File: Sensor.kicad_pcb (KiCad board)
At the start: 2 copper layers, 49.5 x 49.5 mm, 51 parts, among them IC1 STM32L051K8T6, P1 CONN_02X04, P3 CONN_02X04, P4 CONN_01X04, P5 CONN_01X02, Q1 PMosfetGen, Q2 PMosfetGen, Q4 PMosfetGen, Q5 AO3401, SW1 SW_PUSH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

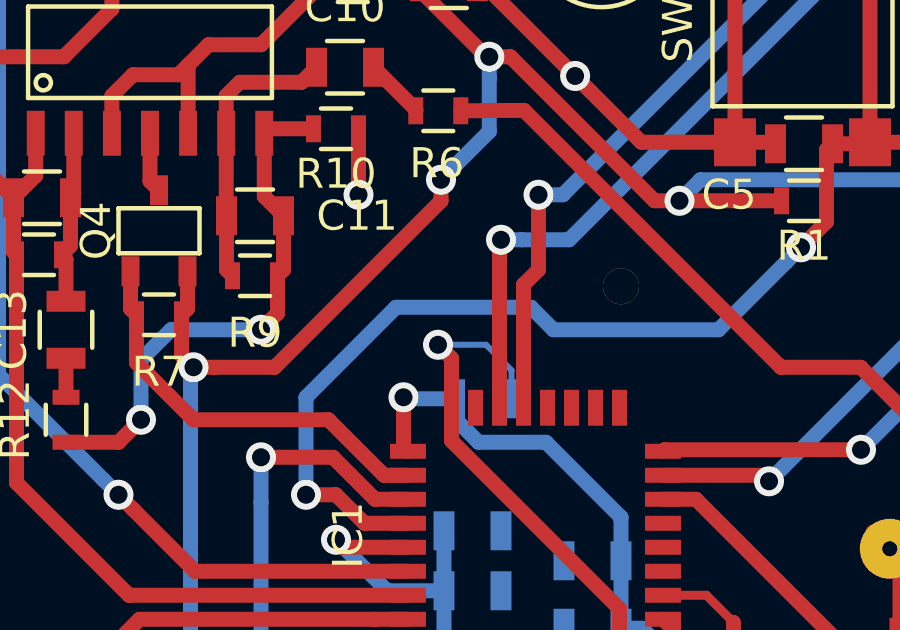
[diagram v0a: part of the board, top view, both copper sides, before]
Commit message: Fix Boot0 pin and add prices per component
Signed-off-by: Philip Luyckx <philip.luyckx@gmail.com>
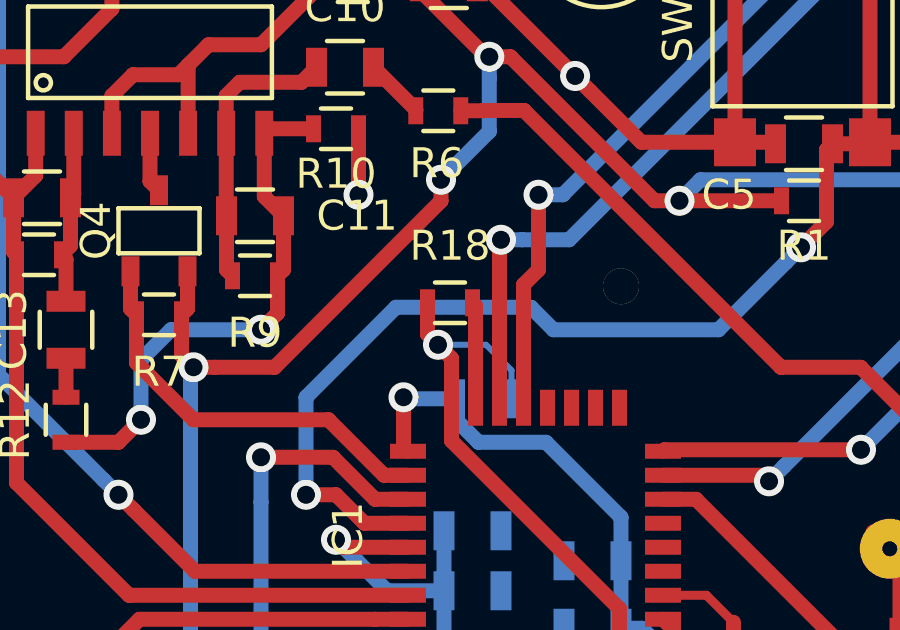
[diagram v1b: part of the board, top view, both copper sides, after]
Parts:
- added R18: 475, Resistors_SMD:R_0603, F.Cu at (137.8, 84.6)
- C12, C15: value C -> 100nF
- Q1, Q2, Q4: value PMosfetGen -> AO3401
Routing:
- net Net-(IC1-Pad31): track 0.00 -> 3.54 mm
- net GND: track 151.5 -> 153.0 mm
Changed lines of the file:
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@@
 (kicad_pcb (version 4) (host pcbnew 4.0.2-4+6225~38~ubuntu15.10.1-stable)
   (general
-    (links 115)
+    (links 117)
     (no_connects 0)
-    (area 109.774999 55.61 191.5 119.575)
+    (area 118.449999 69.199999 168.050001 118.800001)
     (thickness 1.6)
     (drawings 10)
-    (tracks 460)
+    (tracks 464)
     (zones 0)
-    (modules 51)
+    (modules 52)
     (nets 46)
   )
@@
       (effects (font (size 1 1) (thickness 0.15)))
     )
-    (fp_text value C (at 0 2.1) (layer F.Fab)
+    (fp_text value 100nF (at 0 2.1) (layer F.Fab)
       (effects (font (size 1 1) (thickness 0.15)))
     )
@@
       (effects (font (size 1 1) (thickness 0.15)))
     )
-    (fp_text value PMosfetGen (at 0.05 0.05 90) (layer F.Fab) hide
+    (fp_text value AO3401 (at 0.05 0.05 90) (layer F.Fab) hide
       (effects (font (size 1 1) (thickness 0.15)))
     )
@@
       (effects (font (size 1 1) (thickness 0.15)))
     )
-    (fp_text value PMosfetGen (at 0.05 0.05 90) (layer F.Fab) hide
+    (fp_text value AO3401 (at 0.05 0.05 90) (layer F.Fab) hide
       (effects (font (size 1 1) (thickness 0.15)))
     )
@@
       (effects (font (size 1 1) (thickness 0.15)))
     )
-    (fp_text value PMosfetGen (at 0.05 0.05) (layer F.Fab) hide
+    (fp_text value AO3401 (at 0.05 0.05) (layer F.Fab) hide
       (effects (font (size 1 1) (thickness 0.15)))
     )
@@
       (effects (font (size 1 1) (thickness 0.15)))
     )
-    (fp_text value C (at 0 2.1) (layer F.Fab)
+    (fp_text value 100nF (at 0 2.1) (layer F.Fab)
       (effects (font (size 1 1) (thickness 0.15)))
     )
@@
       (net 1 +BATT))
     (model Resistors_SMD.3dshapes/R_0805.wrl
+      (at (xyz 0 0 0))
+      (scale (xyz 1 1 1))
+      (rotate (xyz 0 0 0))
+    )
+  )
+  (module Resistors_SMD:R_0603 (layer F.Cu)
+    (at 137.8 84.6)
+    (descr "Resistor SMD 0603, reflow soldering, Vishay (see dcrcw.pdf)")
+    (tags "resistor 0603")
+    (attr smd)
+    (fp_text reference R18 (at 0 -1.9) (layer F.SilkS)
+      (effects (font (size 1 1) (thickness 0.15)))
+    )
+    (fp_text value 475 (at 0 1.9) (layer F.Fab)
+      (effects (font (size 1 1) (thickness 0.15)))
+    )
+    (fp_line (start -1.3 -0.8) (end 1.3 -0.8) (layer F.CrtYd) (width 0.05))
+    (fp_line (start -1.3 0.8) (end 1.3 0.8) (layer F.CrtYd) (width 0.05))
+    (fp_line (start -1.3 -0.8) (end -1.3 0.8) (layer F.CrtYd) (width 0.05))
+    (fp_line (start 1.3 -0.8) (end 1.3 0.8) (layer F.CrtYd) (width 0.05))
+    (fp_line (start 0.5 0.675) (end -0.5 0.675) (layer F.SilkS) (width 0.15))
+    (fp_line (start -0.5 -0.675) (end 0.5 -0.675) (layer F.SilkS) (width 0.15))
+    (pad 1 smd rect (at -0.75 0) (size 0.5 0.9) (layers F.Cu F.Paste F.Mask)
+      (net 2 GND))
+    (pad 2 smd rect (at 0.75 0) (size 0.5 0.9) (layers F.Cu F.Paste F.Mask)
+      (net 39 "Net-(IC1-Pad31)"))
+    (model Resistors_SMD.3dshapes/R_0603.wrl
       (at (xyz 0 0 0))
       (scale (xyz 1 1 1))
@@
   (segment (start 138.568665 116.340649) (end 134.340649 116.340649) (width 0.5) (layer B.Cu) (net 1))
   (segment (start 134.340649 116.340649) (end 133 115) (width 0.5) (layer B.Cu) (net 1))
+  (segment (start 137.05 84.6) (end 137.05 85.65) (width 0.5) (layer F.Cu) (net 2))
+  (segment (start 137.05 85.65) (end 137.4 86) (width 0.5) (layer F.Cu) (net 2))
   (segment (start 138.71 73.9) (end 138.83 73.9) (width 0.5) (layer F.Cu) (net 2))
   (segment (start 138.83 73.9) (end 141.97 77.04) (width 0.5) (layer F.Cu) (net 2))
@@
   (segment (start 126.53 77.7) (end 127.23 77) (width 0.5) (layer F.Cu) (net 35))
   (segment (start 133.81 73.9) (end 133.81 71.9) (width 0.5) (layer F.Cu) (net 35))
+  (segment (start 138.65 88.1) (end 138.65 84.7) (width 0.5) (layer F.Cu) (net 39))
+  (segment (start 138.65 84.7) (end 138.55 84.6) (width 0.5) (layer F.Cu) (net 39))
   (segment (start 127.15 83.55) (end 127.15 84.8) (width 0.5) (layer F.Cu) (net 41))
   (segment (start 127.15 84.8) (end 127.35 85) (width 0.5) (layer F.Cu) (net 41))

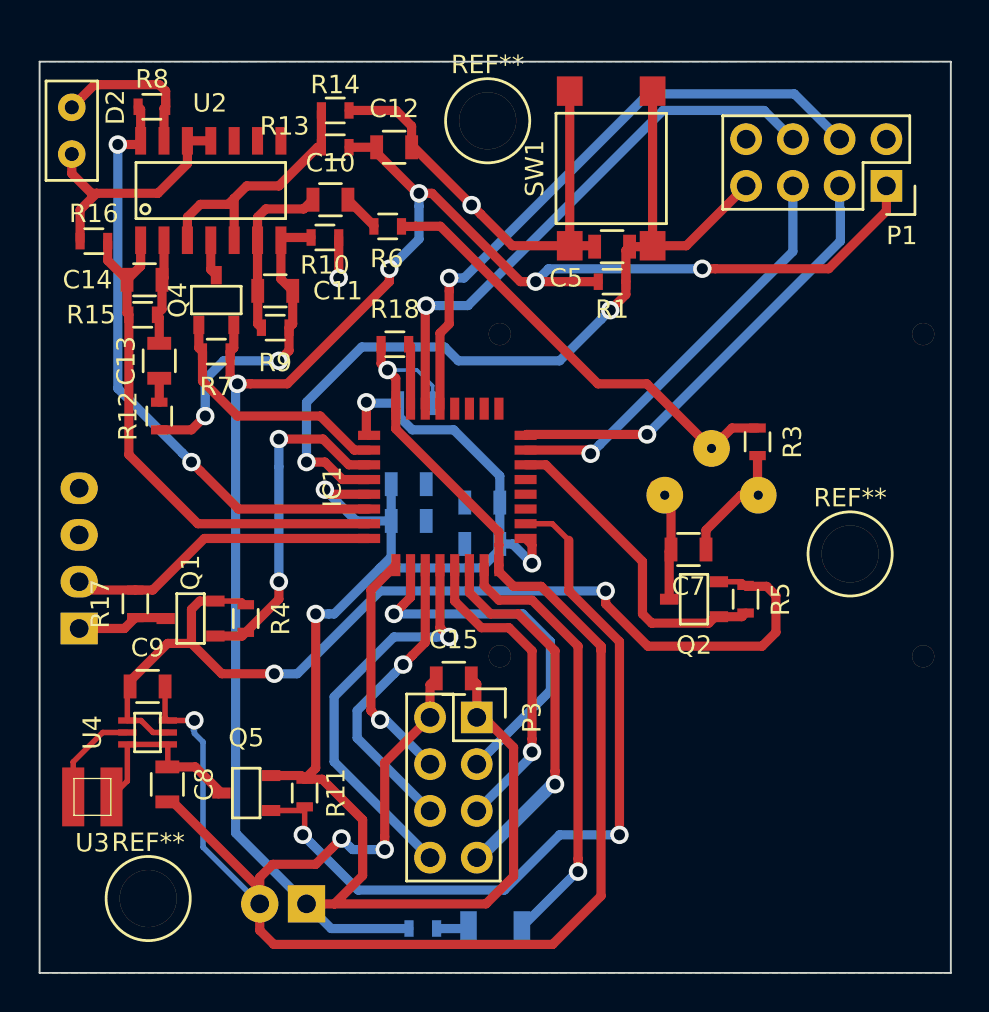
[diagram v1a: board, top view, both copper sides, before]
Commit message: Fix Boot0 pin and mechanical problem with the Fresnel lens
 * Resistor at Boot0 pin not necessary:
     it is only input and can directly connected to ground
 * The capacitors above the cpu on the bottom layer are not
     correctly placed: there is a problem when placing the
     Fresnel lens.

Signed-off-by: Philip Luyckx <philip.luyckx@gmail.com>
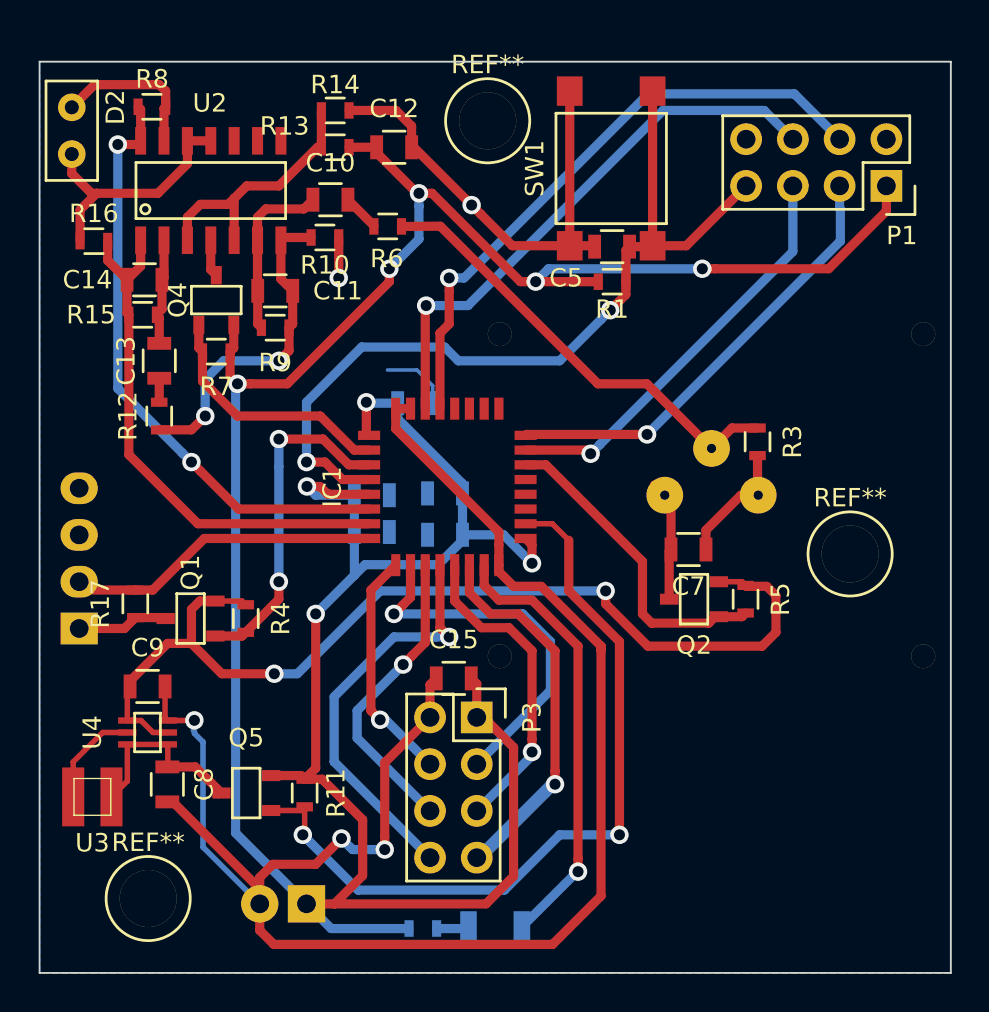
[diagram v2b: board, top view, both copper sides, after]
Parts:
- removed R18: 475, Resistors_SMD:R_0603
- moved C2 2.09 mm to (136.6, 94.8)
- moved C4 2.09 mm to (136.6, 92.8)
- moved C1 2.09 mm to (140.5, 92.7)
- moved C3 2.09 mm to (140.5, 95.0)
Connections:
- IC1 pad 31: Net-(IC1-Pad31) -> GND
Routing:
- net Net-(IC1-Pad31): track 3.54 -> 0.00 mm
- net +BATT: track 180.3 -> 177.1 mm
- net GND: track 153.0 -> 150.0 mm, vias 6 -> 5

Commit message: Finish schematic, assign all footprints for V3
Signed-off-by: pluyckx <philip.luyckx@gmail.com>
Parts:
- removed C1, C10, C13, C7, C8, C9: 10uF, Resistors_SMD:R_0805
- removed C11, C12, C14, C15, C3, C4, C5, C6: 100nF, Resistors_SMD:R_0805
- removed C2: 1uF, Resistors_SMD:R_0805
- removed D1: LED, Resistors_SMD:R_1206
- removed D2: PhotoDiode, CustomModules:PD638C
- removed IC1: STM32L051K8T6, STM32:STM32L051-LQFP32
- removed P1, P3: CONN_02X04, Socket_Strips:Socket_Strip_Straight_2x04
- removed P4: CONN_01X04, Socket_Strips:Socket_Strip_Angled_1x04
- removed P5: CONN_01X02, Socket_Strips:Socket_Strip_Straight_1x02
- removed Q1, Q2, Q4, Q5: AO3401, CustomSmd:SOT23
- removed R1, R13, R14, R3: 100k, Resistors_SMD:R_0603
- removed R10, R12, R16, R6: 10k, Resistors_SMD:R_0603
- removed R11: 47k, Resistors_SMD:R_0603
- removed R15, R9: 1M, Resistors_SMD:R_0603
- removed R17: 1k, Resistors_SMD:R_0603
- removed R2: 475, Resistors_SMD:R_0603
- removed R4, R5, R7: 47.5k, Resistors_SMD:R_0603
- removed R8: 3600, Resistors_SMD:R_0603
- removed REF** (x3): 1pin, Connect:1pin
- removed SW1: SW_PUSH, CustomSmd:MicroSwitch_6x6mm
- removed U1: PIR, CustomModules:PIR
- removed U2: MCP6004, CustomSmd:SOIC-14
- removed U3: EPL3015, CustomInductors:EPL3015
- removed U4: TPS61222, DC_DC_Converters:TPS6122x
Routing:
- net +BATT: track 177.1 -> 0.00 mm, vias 9 -> 0
- net GND: track 150.0 -> 0.00 mm, vias 5 -> 0
- net +5V: track 55.6 -> 0.00 mm, vias 2 -> 0
- net MCU_RST: track 46.2 -> 0.00 mm, vias 2 -> 0
- net Enable5V: track 43.0 -> 0.00 mm, vias 2 -> 0
- net UART_TX: track 33.7 -> 0.00 mm, vias 1 -> 0
- net ADC_Light: track 32.8 -> 0.00 mm, vias 2 -> 0
- net UART_RX: track 30.6 -> 0.00 mm, vias 1 -> 0
- net ADC_Motion: track 29.1 -> 0.00 mm
- net RF_IRQ: track 26.5 -> 0.00 mm, vias 1 -> 0
- net Motion_Out: track 24.8 -> 0.00 mm
- net SWDCLK: track 24.5 -> 0.00 mm, vias 1 -> 0
- net MCU_LED: track 24.1 -> 0.00 mm, vias 1 -> 0
- net SWDIO: track 22.7 -> 0.00 mm, vias 1 -> 0
- net SPI_RF_MISO: track 22.6 -> 0.00 mm, vias 1 -> 0
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
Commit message: Finish routing v4
Signed-off-by: pluyckx <philip.luyckx@gmail.com>
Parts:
- added C1: 10uF, Resistors_SMD:R_0805, F.Cu at (138.1, 101.4)
- added C10: 100nF, Resistors_SMD:R_0805, B.Cu at (124.4, 79.6)
- added C11: 10uF, Resistors_SMD:R_0805, F.Cu at (144.2, 79.4)
- added C12: 10uF, Resistors_SMD:R_0805, F.Cu at (132.2, 78.8)
- added C13: 100nF, Resistors_SMD:R_0805, F.Cu at (130.5, 74.4)
- added C14: 100nF, Resistors_SMD:R_0805, F.Cu at (124.4, 89.6)
- added C15: 10uF, Resistors_SMD:R_0805, F.Cu at (131.0, 83.5)
- added C16: 100nF, Resistors_SMD:R_0805, F.Cu at (129.9, 88.2)
- added C17: 0.1uF, Resistors_SMD:R_0805, F.Cu at (126.6, 92.9)
- added C18: 0.47uF, Resistors_SMD:R_0805, F.Cu at (123.3, 92.9)
- added C19: 10uF, Resistors_SMD:R_0805, F.Cu at (148.1, 71.3)
- added C2: 1uF, Resistors_SMD:R_0805, F.Cu at (144.7, 86.4)
- added C20: 10uF, Resistors_SMD:R_0805, F.Cu at (144.9, 71.3)
- added C3: 100nF, Resistors_SMD:R_0805, F.Cu at (139.5, 100.0)
- added C4: 100nF, Resistors_SMD:R_0805, F.Cu at (144.7, 88.4)
- added C5: 100nF, Resistors_SMD:R_0805, F.Cu at (157.4, 80.6)
- added C6: 100nF, Resistors_SMD:R_0805, F.Cu at (148.8, 90.7)
- added C7: 100nF, Resistors_SMD:R_0805, F.Cu at (145.8, 116.4)
- added C8: 1uF, Resistors_SMD:R_0805, B.Cu at (124.4, 81.7)
- added C9: 100nF, Resistors_SMD:R_0805, B.Cu at (163.9, 74.2)
- added D1: LED, Resistors_SMD:R_1206, F.Cu at (162.2, 98.3)
- added D2: PhotoDiode, CustomModules:PD638C, F.Cu at (124.5, 73.2)
- added IC1: STM32L051K8T6, STM32:STM32L051-LQFP32, F.Cu at (144.1, 95.4)
- added P1: CONN_02X04, Socket_Strips:Socket_Strip_Straight_2x04, B.Cu at (147.1, 114.0)
- added P2: CONN_02X04, Socket_Strips:Socket_Strip_Straight_2x04, F.Cu at (160.1, 94.5)
- added P3: CONN_01X02, Socket_Strips:Socket_Strip_Straight_1x02, F.Cu at (161.5, 116.0)
- added Q1: AO3401, CustomSmd:SOT23, F.Cu at (149.9, 73.7)
- added R1: 100k, Resistors_SMD:R_0603, F.Cu at (154.6, 83.6)
- added R10: 1M, Resistors_SMD:R_0603, F.Cu at (123.1, 87.6)
- added R11: 1M, Resistors_SMD:R_0603, F.Cu at (125.9, 87.6)
- added R12: 1M, Resistors_SMD:R_0603, F.Cu at (130.0, 86.4)
- added R13: 47k, Resistors_SMD:R_0603, F.Cu at (152.9, 73.7)
- added R14: 100k, Resistors_SMD:R_0603, F.Cu at (122.7, 96.2)
- added R2: 10k, Resistors_SMD:R_0603, F.Cu at (156.8, 75.0)
- added R3: 10k, Resistors_SMD:R_0603, F.Cu at (160.2, 75.8)
- added R4: 475, Resistors_SMD:R_0603, F.Cu at (165.8, 98.3)
- added R5: 3600, Resistors_SMD:R_0603, B.Cu at (121.6, 78.1)
- added R6: 100k, Resistors_SMD:R_0603, F.Cu at (141.4, 83.8)
- added R7: 10k, Resistors_SMD:R_0603, F.Cu at (138.4, 83.8)
- added R8: 1M, Resistors_SMD:R_0603, F.Cu at (130.5, 76.2)
- added R9: 10k, Resistors_SMD:R_0603, F.Cu at (131.6, 81.0)
- added SW1: SW_PUSH, CustomSmd:MicroSwitch_6x6mm, F.Cu at (161.8, 80.6)
- added U1: MCP60x4, CustomSmd:SOIC-14, F.Cu at (124.2, 81.2)
- added U2: HTU21D, CustomSmd:HTU21D_QFN, F.Cu at (163.8, 72.7)
- added U3: PIR, CustomModules:PIR, B.Cu at (144.3, 81.2)
- added U4: TPS79718, CustomSmd:SC70, F.Cu at (124.9, 96.0)
- added U5: EPL3015, CustomInductors:EPL3015, F.Cu at (141.9, 74.7)
- added U6: TPS61222, DC_DC_Converters:TPS6122x, F.Cu at (145.7, 73.7)
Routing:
- net +BATT: track 0.00 -> 293.6 mm, vias 0 -> 3
- net +1V8: track 0.00 -> 80.2 mm, vias 0 -> 5
- net GND: track 0.00 -> 71.2 mm, vias 0 -> 11
- net RF_CE: track 0.00 -> 38.0 mm
- net RF_CSN: track 0.00 -> 37.0 mm
- net UART_TX: track 0.00 -> 36.5 mm, vias 0 -> 2
- net Enable5V: track 0.00 -> 35.1 mm, vias 0 -> 2
- net UART_RX: track 0.00 -> 34.3 mm, vias 0 -> 1
- net SPI_RF_MOSI: track 0.00 -> 33.9 mm, vias 0 -> 2
- net MCU_RST: track 0.00 -> 32.0 mm
- net ADC_Light: track 0.00 -> 31.9 mm, vias 0 -> 2
- net HTU21_SCK: track 0.00 -> 31.6 mm, vias 0 -> 2
- net SPI_RF_SCK: track 0.00 -> 29.8 mm
- net HTU21_SDA: track 0.00 -> 28.6 mm, vias 0 -> 2
- net SPI_RF_MISO: track 0.00 -> 25.1 mm
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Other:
- net class BoostConv: clearance 0.2 -> 0.254
- net class Default: clearance 0.25 -> 0.254
- net class GND removed
- net class Opamp: clearance 0.25 -> 0.254
- net class mcu: clearance 0.2 -> 0.254
- rule trace_clearance: 0.25 -> 0.254

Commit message: Update some routing
Signed-off-by: pluyckx <philip.luyckx@gmail.com>
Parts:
- added R15: 1M, Resistors_SMD:R_0603, F.Cu at (123.8, 88.5)
- added R16: 1M, Resistors_SMD:R_0603, F.Cu at (126.9, 88.5)
- added R17: 1.6M, Resistors_SMD:R_0603, B.Cu at (121.5, 83.8)
- moved C14 1.60 mm to (124.5, 91.2)
- moved R10 1.06 mm to (123.8, 86.8)
- moved R11 1.05 mm to (126.6, 86.8)
- moved C17 0.40 mm to (126.6, 93.3)
- moved C18 0.40 mm to (123.3, 93.3)
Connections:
- IC1 pad 6: ADC_Light -> DIG_Motion
- IC1 pad 7: ADC_Motion -> ADC_Light
- IC1 pad 8: Net-(IC1-Pad8) -> ADC_Motion
- U1 pad 12: Motion_Offset -> Net-(R15-Pad2)
- U1 pad 13: Net-(U1-Pad13) -> ADC_Motion
- U1 pad 14: Net-(U1-Pad13) -> DIG_Motion
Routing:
- net DIG_Motion: track 0.00 -> 35.6 mm, vias 0 -> 3
- net ADC_Motion: track 21.3 -> 38.1 mm, vias 0 -> 2
- net Net-(R15-Pad2): track 0.00 -> 12.5 mm, vias 0 -> 1
- net Motion_Offset: track 16.6 -> 11.5 mm
- net +BATT: track 293.6 -> 296.0 mm
- net GND: track 71.2 -> 73.3 mm
- net Net-(U1-Pad13): track 1.27 -> 0.00 mm
- net ADC_Light: track 31.9 -> 31.2 mm, vias 2 -> 3
- net +1V8: track 80.2 -> 79.7 mm
